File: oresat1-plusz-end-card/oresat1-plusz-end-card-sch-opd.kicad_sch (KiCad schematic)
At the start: 63 parts, among them Q1 DMP2240UDM-7, Q11 DMP2240UDM-7, Q2 DMN3028LQ-7, Q3 DMN3028LQ-7, Q4 DMN3028LQ-7, Q6 DMN3028LQ-7, Q9 DMP2240UDM-7, U11 MIC842LYC5, U12 MIC842LYC5, U2 MAX7310, U201 TS5A21366, U203 TS5A21366

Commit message: Polishing schematic, syncing, polishing layout, added releases folder, updating makefile
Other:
- note added: ""DEPLOY""
- note added: "1206"
- moved on the sheet: R106
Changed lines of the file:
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@@
 	)
 	(rectangle
-		(start 326.39 99.06)
-		(end 347.98 114.3)
+		(start 317.5 100.33)
+		(end 345.44 115.57)
+		(stroke
+			(width 0)
+			(type default)
+		)
+		(fill
+			(type none)
+		)
+	)
+	(rectangle
+		(start 317.5 121.92)
+		(end 345.44 146.05)
 		(stroke
 			(width 0)
@@
 	(text "DNP for testing\nInstall for flight"
 		(exclude_from_sim no)
-		(at 339.598 110.998 0)
+		(at 331.216 111.506 0)
 		(effects
 			(font
@@
 		)
 	)
+	(text "1206"
+		(exclude_from_sim no)
+		(at 336.042 106.934 0)
+		(effects
+			(font
+				(size 1.27 1.27)
+			)
+		)
+	)
 	(text "PAC100007508FA1000"
 		(exclude_from_sim no)
@@
 	(text "Address 0x14"
 		(exclude_from_sim no)
-		(at 104.14 25.908 0)
+		(at 114.808 26.416 0)
 		(effects
 			(font
 				(size 1.27 1.27)
+				(thickness 0.254)
+				(bold yes)
 			)
 			(justify left bottom)
@@
 		)
 	)
+	(text "\"DEPLOY\""
+		(exclude_from_sim no)
+		(at 363.474 103.124 0)
+		(effects
+			(font
+				(size 1.27 1.27)
+			)
+		)
+	)
 	(text "Helical Antenna Deployer"
 		(exclude_from_sim no)
@@
 		)
 	)
-	(polyline
-		(pts
-			(xy 345.44 146.05) (xy 317.5 146.05)
-		)
-		(stroke
-			(width 0)
-			(type default)
-		)
-	)
 	(wire
 		(pts
@@
 		)
 	)
-	(polyline
-		(pts
-			(xy 345.44 116.84) (xy 345.44 146.05)
-		)
-		(stroke
-			(width 0)
-			(type default)
-		)
-	)
 	(wire
 		(pts
@@
 		)
 	)
-	(polyline
-		(pts
-			(xy 317.5 146.05) (xy 317.5 116.84)
-		)
-		(stroke
-			(width 0)
-			(type default)
-		)
-	)
 	(wire
 		(pts
-			(xy 331.47 107.95) (xy 331.47 123.19)
+			(xy 331.47 106.68) (xy 331.47 123.19)
 		)
 		(stroke
@@
 	(wire
 		(pts
-			(xy 331.47 88.9) (xy 331.47 102.87)
-		)
-		(stroke
-			(width 0)
-			(type default)
-		)
-	)
-	(polyline
-		(pts
-			(xy 317.5 116.84) (xy 345.44 116.84)
+			(xy 331.47 88.9) (xy 331.47 101.6)
 		)
 		(stroke
@@
 			(font
 				(size 1.27 1.27)
+				(thickness 0.254)
+				(bold yes)
 			)
 			(justify right)
@@
 			(font
 				(size 1.27 1.27)
+				(thickness 0.254)
+				(bold yes)
 			)
 			(justify right)
@@
 			(font
 				(size 1.27 1.27)
+				(thickness 0.254)
+				(bold yes)
 			)
 			(justify right)
@@
 		(dnp no)
 		(property "Reference" "C4"
-			(at 151.638 124.206 0)
+			(at 148.59 120.142 90)
 			(show_name no)
 			(do_not_autoplace no)
@@
 		)
 		(property "Value" "100n"
-			(at 147.828 124.206 0)
+			(at 147.828 122.174 90)
 			(show_name no)
 			(do_not_autoplace no)
@@
 	(symbol
 		(lib_id "Device:R_Small_US")
-		(at 331.47 105.41 0)
+		(at 331.47 104.14 0)
 		(mirror y)
 		(unit 1)
@@
 		(dnp no)
 		(property "Reference" "R106"
-			(at 334.01 104.775 0)
+			(at 333.756 102.616 0)
 			(show_name no)
 			(do_not_autoplace no)
@@
 		)
 		(property "Value" "0"
-			(at 334.01 107.315 0)
+			(at 333.756 104.648 0)
 			(show_name no)
 			(do_not_autoplace no)
@@
 		)
 		(property "Footprint" "oresat-passives:1206-C"
-			(at 331.47 105.41 0)
+			(at 331.47 104.14 0)
 			(hide yes)
 			(show_name no)
@@
 		)
 		(property "Datasheet" "https://www.seielect.com/catalog/SEI-RMCF_RMCP.pdf"
-			(at 331.47 105.41 0)
+			(at 331.47 104.14 0)
 			(hide yes)
 			(show_name no)
@@
 		)
 		(property "Description" "0 Ohms Jumper Chip Resistor 1206 (3216 Metric) Automotive AEC-Q200 Thick Film"
-			(at 331.47 105.41 0)
+			(at 331.47 104.14 0)
 			(hide yes)
 			(show_name no)
@@
 		)
 		(property "DPN" "738-RMCF1206ZG0R00CT-ND"
-			(at 331.47 105.41 0)
+			(at 331.47 104.14 0)
 			(hide yes)
 			(show_name no)
@@
 		)
 		(property "MFR" "Stackpole Electronics"
-			(at 331.47 105.41 0)
+			(at 331.47 104.14 0)
 			(hide yes)
 			(show_name no)
@@
 		)
 		(property "MPN" "RMCF1206ZG0R00"
-			(at 331.47 105.41 0)
+			(at 331.47 104.14 0)
 			(hide yes)
 			(show_name no)
@@
 		)
 		(property "DIS" "DigiKey"
-			(at 331.47 105.41 0)
+			(at 331.47 104.14 0)
 			(hide yes)
 			(show_name no)
@@
 		(dnp no)
 		(property "Reference" "R105"
-			(at 271.018 71.12 0)
+			(at 269.494 71.374 0)
 			(show_name no)
 			(do_not_autoplace no)
@@
 		)
 		(property "Value" "10k"
-			(at 271.018 73.66 0)
+			(at 268.224 73.66 0)
 			(show_name no)
 			(do_not_autoplace no)
@@
 		(dnp no)
 		(property "Reference" "C10"
-			(at 152.908 173.736 0)
+			(at 149.098 169.418 90)
 			(show_name no)
 			(do_not_autoplace no)
@@
 		)
 		(property "Value" "100n"
-			(at 149.098 173.736 0)
+			(at 148.844 171.45 90)
 			(show_name no)
 			(do_not_autoplace no)
@@
 		(dnp no)
 		(property "Reference" "R1"
-			(at 330.2 124.46 0)
+			(at 336.296 123.952 0)
 			(show_name no)
 			(do_not_autoplace no)
@@
 		)
 		(property "Value" "7.5  1W"
-			(at 332.74 123.19 90)
+			(at 342.392 126.492 0)
 			(show_name no)
 			(do_not_autoplace no)
@@
 		(dnp no)
 		(property "Reference" "C204"
-			(at 275.336 57.658 0)
+			(at 281.178 53.848 0)
 			(show_name no)
 			(do_not_autoplace no)
@@
 		)
 		(property "Value" "100n"
-			(at 275.336 53.848 0)
+			(at 281.178 57.912 0)
 			(show_name no)
 			(do_not_autoplace no)

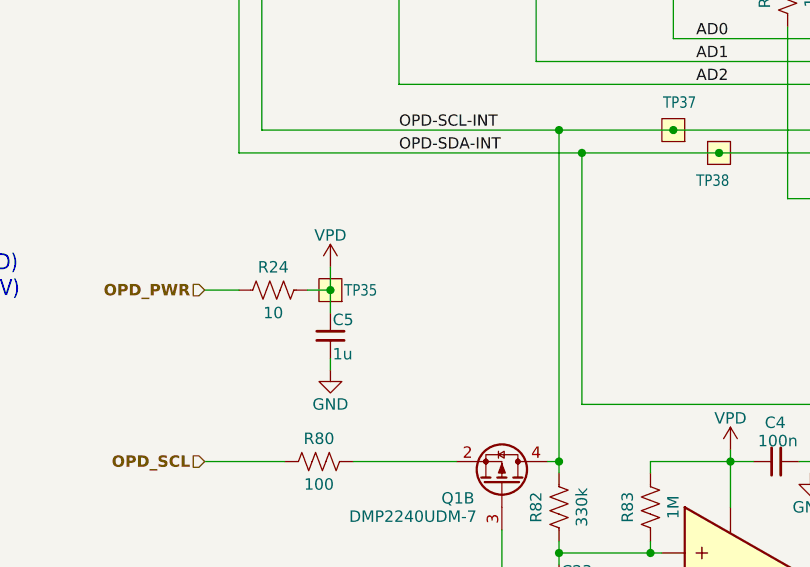
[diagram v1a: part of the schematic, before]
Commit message: Feedback from Pete: make consistent with -Z end card. Changed date, too.
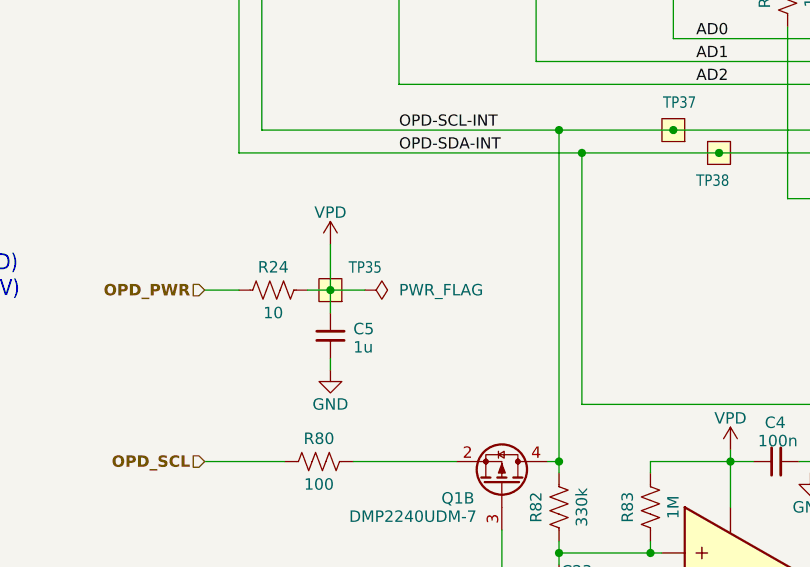
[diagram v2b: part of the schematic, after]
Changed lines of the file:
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@@
 	(title_block
 		(title "OreSat1 +Z End Card")
-		(date "2026-09-22")
+		(date "2026-09-25")
 		(rev "v1.2")
 		(company "Portland State Aerospace Society")
@@
 	(wire
 		(pts
+			(xy 100.33 105.41) (xy 104.14 105.41)
+		)
+		(stroke
+			(width 0)
+			(type default)
+		)
+	)
+	(wire
+		(pts
 			(xy 233.68 92.71) (xy 233.68 86.36)
 		)
@@
 	(wire
 		(pts
-			(xy 100.33 105.41) (xy 100.33 102.87)
+			(xy 100.33 105.41) (xy 100.33 100.33)
 		)
 		(stroke
@@
 		(dnp no)
 		(property "Reference" "TP35"
-			(at 101.854 106.172 0)
+			(at 102.362 103.632 0)
 			(show_name no)
 			(do_not_autoplace no)
@@
 	(symbol
 		(lib_id "oresat-power:VPD")
-		(at 100.33 102.87 0)
+		(at 100.33 100.33 0)
 		(unit 1)
 		(body_style 1)
@@
 		(dnp no)
 		(property "Reference" "#VPD06"
-			(at 100.33 102.87 0)
+			(at 100.33 100.33 0)
 			(hide yes)
 			(show_name no)
@@
 		)
 		(property "Value" "VPD"
-			(at 100.33 100.076 0)
+			(at 100.33 97.536 0)
 			(show_name no)
 			(do_not_autoplace no)
@@
 		)
 		(property "Footprint" ""
-			(at 100.33 102.87 0)
+			(at 100.33 100.33 0)
 			(hide yes)
 			(show_name no)
@@
 		)
 		(property "Datasheet" ""
-			(at 100.33 102.87 0)
+			(at 100.33 100.33 0)
 			(hide yes)
 			(show_name no)
@@
 		)
 		(property "Description" "Power symbol creates a global label with name \"VPD\""
-			(at 100.33 102.87 0)
+			(at 100.33 100.33 0)
 			(hide yes)
 			(show_name no)
@@
 	)
 	(symbol
+		(lib_id "power:PWR_FLAG")
+		(at 104.14 105.41 270)
+		(unit 1)
+		(body_style 1)
+		(exclude_from_sim no)
+		(in_bom yes)
+		(on_board yes)
+		(in_pos_files yes)
+		(dnp no)
+		(property "Reference" "#FLG01"
+			(at 106.045 105.41 0)
+			(hide yes)
+			(show_name no)
+			(do_not_autoplace no)
+			(effects
+				(font
+					(size 1.27 1.27)
+				)
+			)
+		)
+		(property "Value" "PWR_FLAG"
+			(at 107.95 105.4099 90)
+			(show_name no)
+			(do_not_autoplace no)
+			(effects
+				(font
+					(size 1.27 1.27)
+				)
+				(justify left)
+			)
+		)
+		(property "Footprint" "Package_SO:TSSOP-28_4.4x9.7mm_P0.65mm"
+			(at 104.14 105.41 0)
+			(hide yes)
+			(show_name no)
+			(do_not_autoplace no)
+			(effects
+				(font
+					(size 1.27 1.27)
+				)
+			)
+		)
+		(property "Datasheet" ""
+			(at 104.14 105.41 0)
+			(hide yes)
+			(show_name no)
+			(do_not_autoplace no)
+			(effects
+				(font
+					(size 1.27 1.27)
+				)
+			)
+		)
+		(property "Description" "Special symbol for telling ERC where power comes from"
+			(at 104.14 105.41 0)
+			(hide yes)
+			(show_name no)
+			(do_not_autoplace no)
+			(effects
+				(font
+					(size 1.27 1.27)
+				)
+			)
+		)
+		(pin "1"
+		)
+		(instances
+			(project "oresat1-plusz-end-card"
+				(path "/f7595184-4323-4ed9-b19e-5e32e3c6e76f/00d1c146-41ee-47bc-806e-4a57139ad2b4"
+					(reference "#FLG01")
+					(unit 1)
+				)
+			)
+		)
+	)
+	(symbol
 		(lib_id "Device:R_US")
 		(at 125.73 129.54 180)
@@
 		(dnp no)
 		(property "Reference" "C5"
-			(at 100.584 108.712 0)
+			(at 102.87 109.728 0)
 			(show_name no)
 			(do_not_autoplace no)
@@
 		)
 		(property "Value" "1u"
-			(at 100.584 112.522 0)
+			(at 102.87 111.76 0)
 			(show_name no)
 			(do_not_autoplace no)

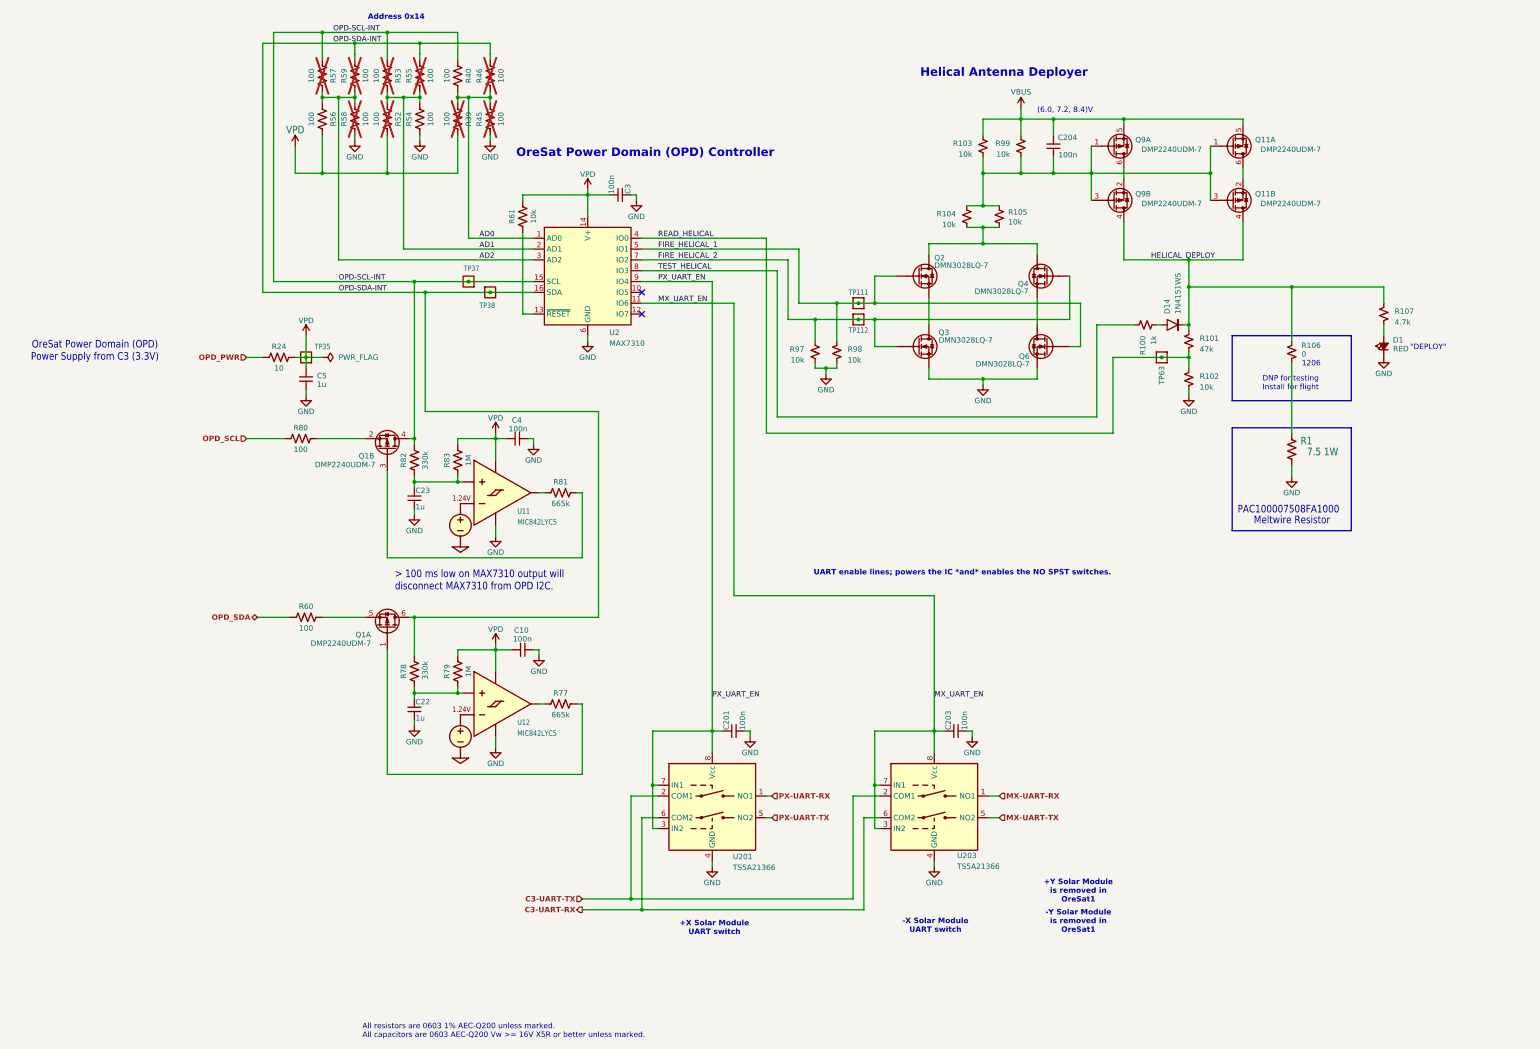
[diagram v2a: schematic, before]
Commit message: v1.2 for fab (hopefully)
Re-Added UART switches for PY and MY (why were they removed?) and cleaned up schematic and routing a bit.
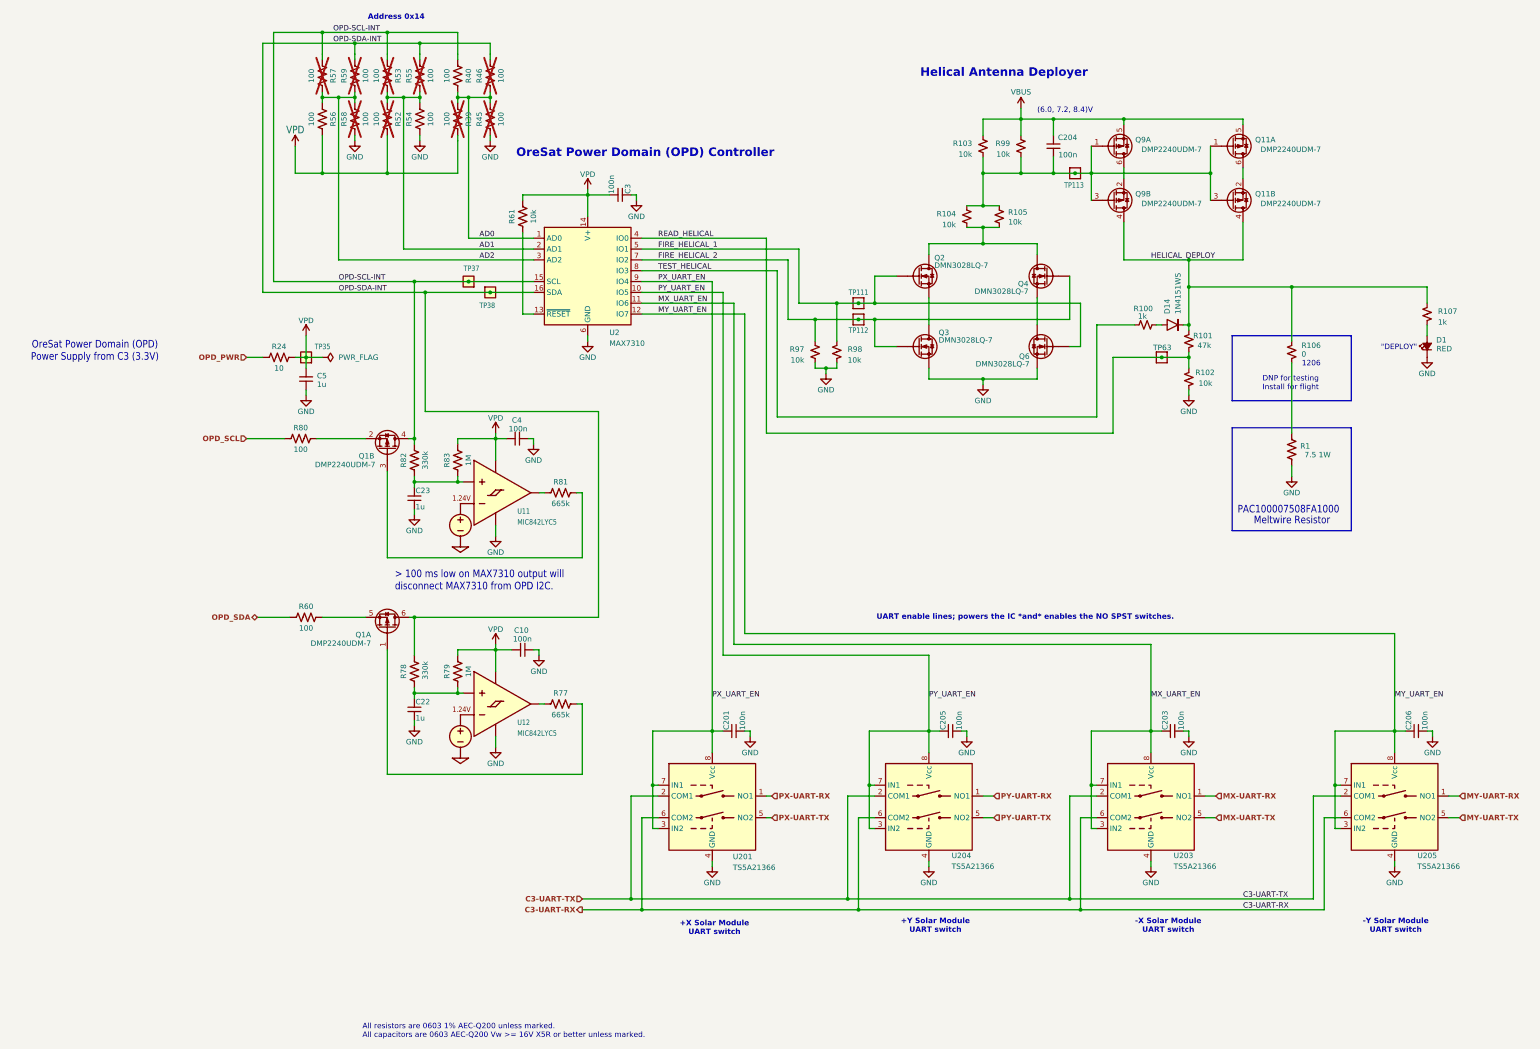
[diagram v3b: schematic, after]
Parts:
- added C205, C206: 100n, oresat-passives:0603-C-NOSILK, symbol Device:C_Small
- added TP113: Test-Point, oresat-misc:TestPoint_Pad_D1.0mm, symbol oresat-misc:Test-Point-1mm-round
- added U204, U205: TS5A21366, Package_SO:VSSOP-8_2.3x2mm_P0.5mm, symbol oresat-ics:TS5A21366
- R100, R101, R102, R103, R104, R105, R97, R98, R99: footprint Resistor_SMD:R_0603_1608Metric -> oresat-passives:0603-C-NOSILK
- R107: value 4.7k -> 1k; DPN RMCF0603FT4K70CT-ND -> RMCF0603FT1K00CT-ND; MFR Stackpole Electronics -> Stackpole Electronics Inc; MPN RMCF0603FT4K70 -> RMCF0603FT1K00
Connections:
- net C3-UART-RX: now also U204.6 (COM2), U205.6 (COM2)
- net C3-UART-TX: now also U204.2 (COM1), U205.2 (COM1)
- net GND: now also C205.2, C206.2, U204.4 (GND), U205.4 (GND)
- net at C204.1, Q11.1 (G), Q11.3 (G)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: now also TP113.1
- net PY_UART_EN: now reaches U2.10 (IO5)
- net PY_UART_EN: now also C205.1, U204.3 (IN2), U204.7 (IN1), U204.8 (Vcc)
- net MY_UART_EN: now reaches U2.12 (IO7)
- net MY_UART_EN: now also C206.1, U205.3 (IN2), U205.7 (IN1), U205.8 (Vcc)
- new net MY-UART-RX: U205.1 (NO1)
- new net MY-UART-TX: U205.5 (NO2)
- new net PY-UART-RX: U204.1 (NO1)
- new net PY-UART-TX: U204.5 (NO2)
- no-connect marks 2 -> 0
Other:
- note added: "+Y Solar Module UART switch"
- note added: "-Y Solar Module UART switch"
- note removed: "+Y Solar Module is removed in OreSat1"
- note removed: "-Y Solar Module is removed in OreSat1"
- moved on the sheet: C203, D1, R107, U203
